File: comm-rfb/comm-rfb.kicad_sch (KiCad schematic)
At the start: 6 parts, among them J1 PC104_Connector

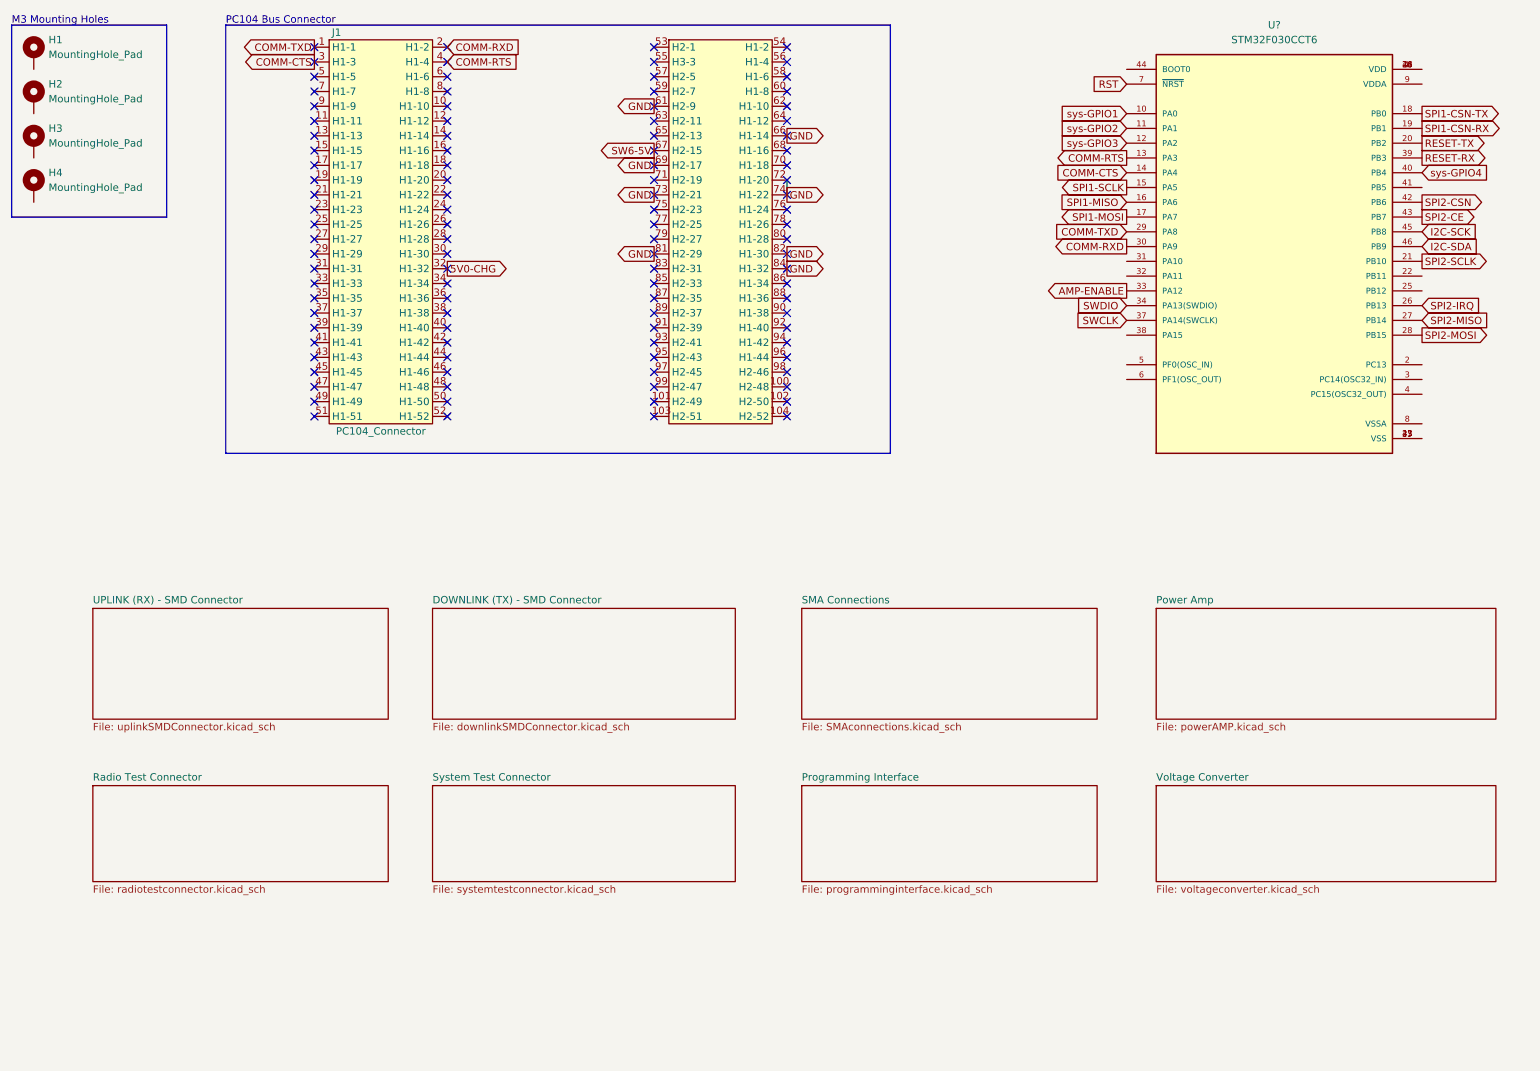
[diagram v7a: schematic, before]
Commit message: started current and voltage converter
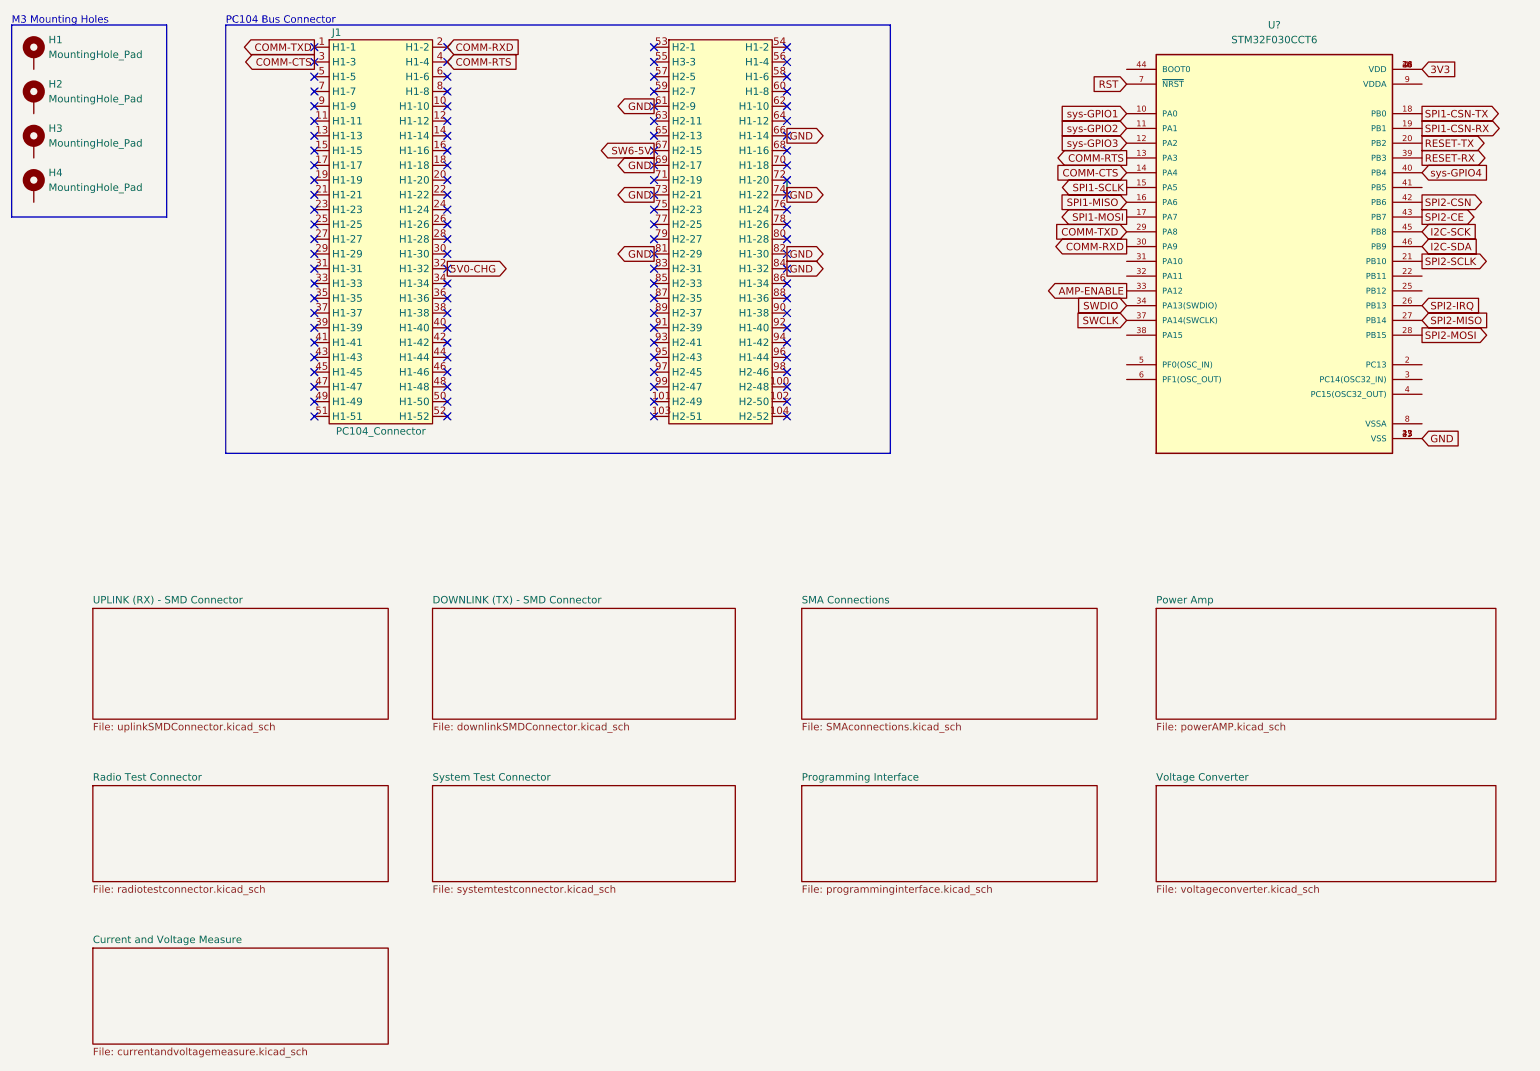
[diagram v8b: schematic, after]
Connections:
- net GND: now also U?.23 (VSS), U?.35 (VSS), U?.47 (VSS)
- net 3V3: now reaches U?.1 (VDD), U?.24 (VDD), U?.36 (VDD), U?.48 (VDD)
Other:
- added sheet Current and Voltage Measure (currentandvoltagemeasure.kicad_sch)
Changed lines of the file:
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@@
+    )
+  )
+  (global_label "GND" (shape input) (at 256.54 86.36 0) (fields_autoplaced)
+    (effects (font (size 1.27 1.27)) (justify left))
+    (property "Intersheet References" "${INTERSHEET_REFS}" (id 0) (at 262.8236 86.2806 0)
+      (effects (font (size 1.27 1.27)) (justify left) hide)
     )
   )
@@
     (effects (font (size 1.27 1.27)) (justify left))
     (property "Intersheet References" "${INTERSHEET_REFS}" (id 0) (at 102.1383 18.9706 0)
+      (effects (font (size 1.27 1.27)) (justify left) hide)
+    )
+  )
+  (global_label "3V3" (shape input) (at 256.54 22.86 0) (fields_autoplaced)
+    (effects (font (size 1.27 1.27)) (justify left))
+    (property "Intersheet References" "${INTERSHEET_REFS}" (id 0) (at 262.4607 22.7806 0)
       (effects (font (size 1.27 1.27)) (justify left) hide)
     )
@@
     )
   )
+  (sheet (at 27.94 173.99) (size 50.8 16.51) (fields_autoplaced)
+    (stroke (width 0.1524) (type solid) (color 0 0 0 0))
+    (fill (color 0 0 0 0.0000))
+    (property "Sheet name" "Current and Voltage Measure" (id 0) (at 27.94 173.2784 0)
+      (effects (font (size 1.27 1.27)) (justify left bottom))
+    )
+    (property "Sheet file" "currentandvoltagemeasure.kicad_sch" (id 1) (at 27.94 191.0846 0)
+      (effects (font (size 1.27 1.27)) (justify left top))
+    )
+  )
   (sheet (at 210.82 146.05) (size 58.42 16.51) (fields_autoplaced)
     (stroke (width 0.1524) (type solid) (color 0 0 0 0))
@@
     (path "/edc7eefe-12bb-4425-b51a-4d6eb34cbded" (page "8"))
     (path "/c253291c-bb52-4e8f-af5c-cbf2e48e8d2a" (page "9"))
+    (path "/af76af4b-bf43-488f-80f3-ce4990a75ce5" (page "10"))
   )
   (symbol_instances
